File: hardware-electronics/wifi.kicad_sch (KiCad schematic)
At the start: 22 parts, among them J4 CONMHF1-SMD-T, U1 RTL8188FTV-VC-CG, Y5 ABM8-40.000MHZ-B2-T

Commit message: [#17] USB routing plan WIP
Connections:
- net +3V3_wifi: now also R38.1
- net GND: no longer R38.1
- net at U1.23 (LED/GPIO4): now also D4.1 (K); no longer D4.2 (A)
- net at R38.2: now also D4.2 (A); no longer D4.1 (K)
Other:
- moved on the sheet: D4
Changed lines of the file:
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@@
 			)
 		)
-		(property "Datasheet" ""
+		(property "Datasheet" "https://xonstorage.blob.core.windows.net/pdf/realtek_rtl8188ftvvccg_apr22_xonlink.pdf"
 			(at 144.78 96.52 0)
 			(effects
@@
 	)
 	(symbol
+		(lib_id "power:+3V3")
+		(at 93.98 104.14 90)
+		(unit 1)
+		(exclude_from_sim no)
+		(in_bom yes)
+		(on_board yes)
+		(dnp no)
+		(fields_autoplaced yes)
+		(property "Reference" "#PWR0110"
+			(at 97.79 104.14 0)
+			(effects
+				(font
+					(size 1.27 1.27)
+				)
+				(hide yes)
+			)
+		)
+		(property "Value" "+3V3_wifi"
+			(at 90.17 104.1399 90)
+			(effects
+				(font
+					(size 1.27 1.27)
+				)
+				(justify left)
+			)
+		)
+		(property "Footprint" ""
+			(at 93.98 104.14 0)
+			(effects
+				(font
+					(size 1.27 1.27)
+				)
+				(hide yes)
+			)
+		)
+		(property "Datasheet" ""
+			(at 93.98 104.14 0)
+			(effects
+				(font
+					(size 1.27 1.27)
+				)
+				(hide yes)
+			)
+		)
+		(property "Description" "Power symbol creates a global label with name \"+3V3\""
+			(at 93.98 104.14 0)
+			(effects
+				(font
+					(size 1.27 1.27)
+				)
+				(hide yes)
+			)
+		)
+		(pin "1"
+		)
+		(instances
+			(project "M2SmartHome"
+				(path "/da663dec-9e91-4003-a791-431d460ad63c/7a341d5c-2113-408f-a1b4-1e4771333f4d"
+					(reference "#PWR0110")
+					(unit 1)
+				)
+			)
+		)
+	)
+	(symbol
 		(lib_id "M2SmartHomeSymbols:04025A270FAT2A")
 		(at 153.67 163.83 90)
@@
 	(symbol
 		(lib_id "M2SmartHomeSymbols:KP-1608CGCK")
-		(at 111.76 104.14 0)
+		(at 111.76 104.14 180)
 		(unit 1)
 		(exclude_from_sim no)
@@
 		(fields_autoplaced yes)
 		(property "Reference" "D4"
-			(at 110.1725 111.76 0)
+			(at 113.3475 96.52 0)
 			(effects
 				(font
@@
 		)
 		(property "Value" "LED"
-			(at 110.1725 109.22 0)
+			(at 113.3475 99.06 0)
 			(effects
 				(font
@@
 					(unit 1)
 				)
-			)
-		)
-	)
-	(symbol
-		(lib_id "power:GND")
-		(at 93.98 104.14 270)
-		(unit 1)
-		(exclude_from_sim no)
-		(in_bom yes)
-		(on_board yes)
-		(dnp no)
-		(fields_autoplaced yes)
-		(property "Reference" "#PWR0126"
-			(at 87.63 104.14 0)
-			(effects
-				(font
-					(size 1.27 1.27)
-				)
-				(hide yes)
-			)
-		)
-		(property "Value" "GND"
-			(at 90.17 104.1401 90)
-			(effects
-				(font
-					(size 1.27 1.27)
-				)
-				(justify right)
-			)
-		)
-		(property "Footprint" ""
-			(at 93.98 104.14 0)
-			(effects
-				(font
-					(size 1.27 1.27)
-				)
-				(hide yes)
-			)
-		)
-		(property "Datasheet" ""
-			(at 93.98 104.14 0)
-			(effects
-				(font
-					(size 1.27 1.27)
-				)
-				(hide yes)
-			)
-		)
-		(property "Description" "Power symbol creates a global label with name \"GND\" , ground"
-			(at 93.98 104.14 0)
-			(effects
-				(font
-					(size 1.27 1.27)
-				)
-				(hide yes)
-			)
-		)
-		(pin "1"
-		)
-		(instances
-			(project "M2SmartHome"
-				(path "/da663dec-9e91-4003-a791-431d460ad63c/7a341d5c-2113-408f-a1b4-1e4771333f4d"
-					(reference "#PWR0126")
-					(unit 1)
-				)

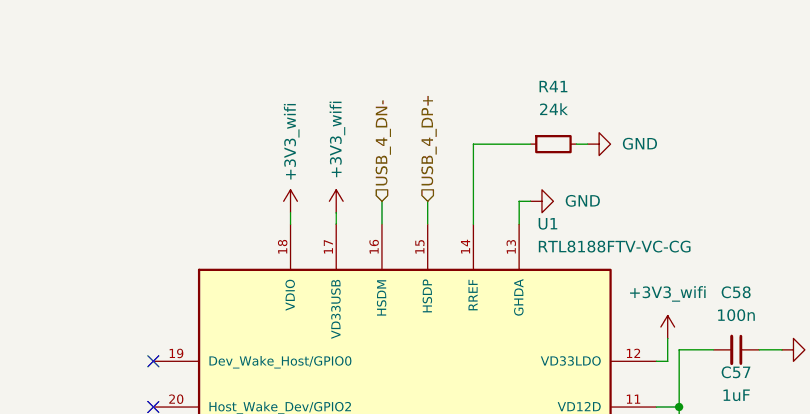
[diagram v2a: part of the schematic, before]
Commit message: [#17] SCH update USB net names
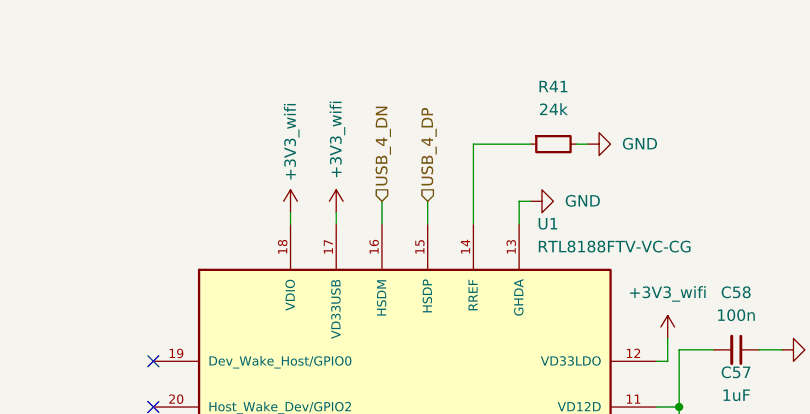
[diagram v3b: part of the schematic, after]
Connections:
- net USB_4_DN- renamed USB_4_DN
- net USB_4_DP+ renamed USB_4_DP
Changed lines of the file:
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@@
 		)
 	)
-	(hierarchical_label "USB_4_DP+"
+	(hierarchical_label "USB_4_DP"
 		(shape input)
 		(at 147.32 66.04 90)
@@
 		)
 	)
-	(hierarchical_label "USB_4_DN-"
+	(hierarchical_label "USB_4_DN"
 		(shape input)
 		(at 142.24 66.04 90)

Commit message: [#20] PCB DRC warnings WIP fix missing footprints
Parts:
- L4: footprint M2SmartHomeFootprints:L_0201_0603Metric -> M2SmartHomeFootprints:L_0201
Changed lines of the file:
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@@
 			)
 		)
-		(property "Footprint" "M2SmartHomeFootprints:L_0201_0603Metric"
+		(property "Footprint" "M2SmartHomeFootprints:L_0201"
 			(at 200.66 121.92 0)
 			(effects

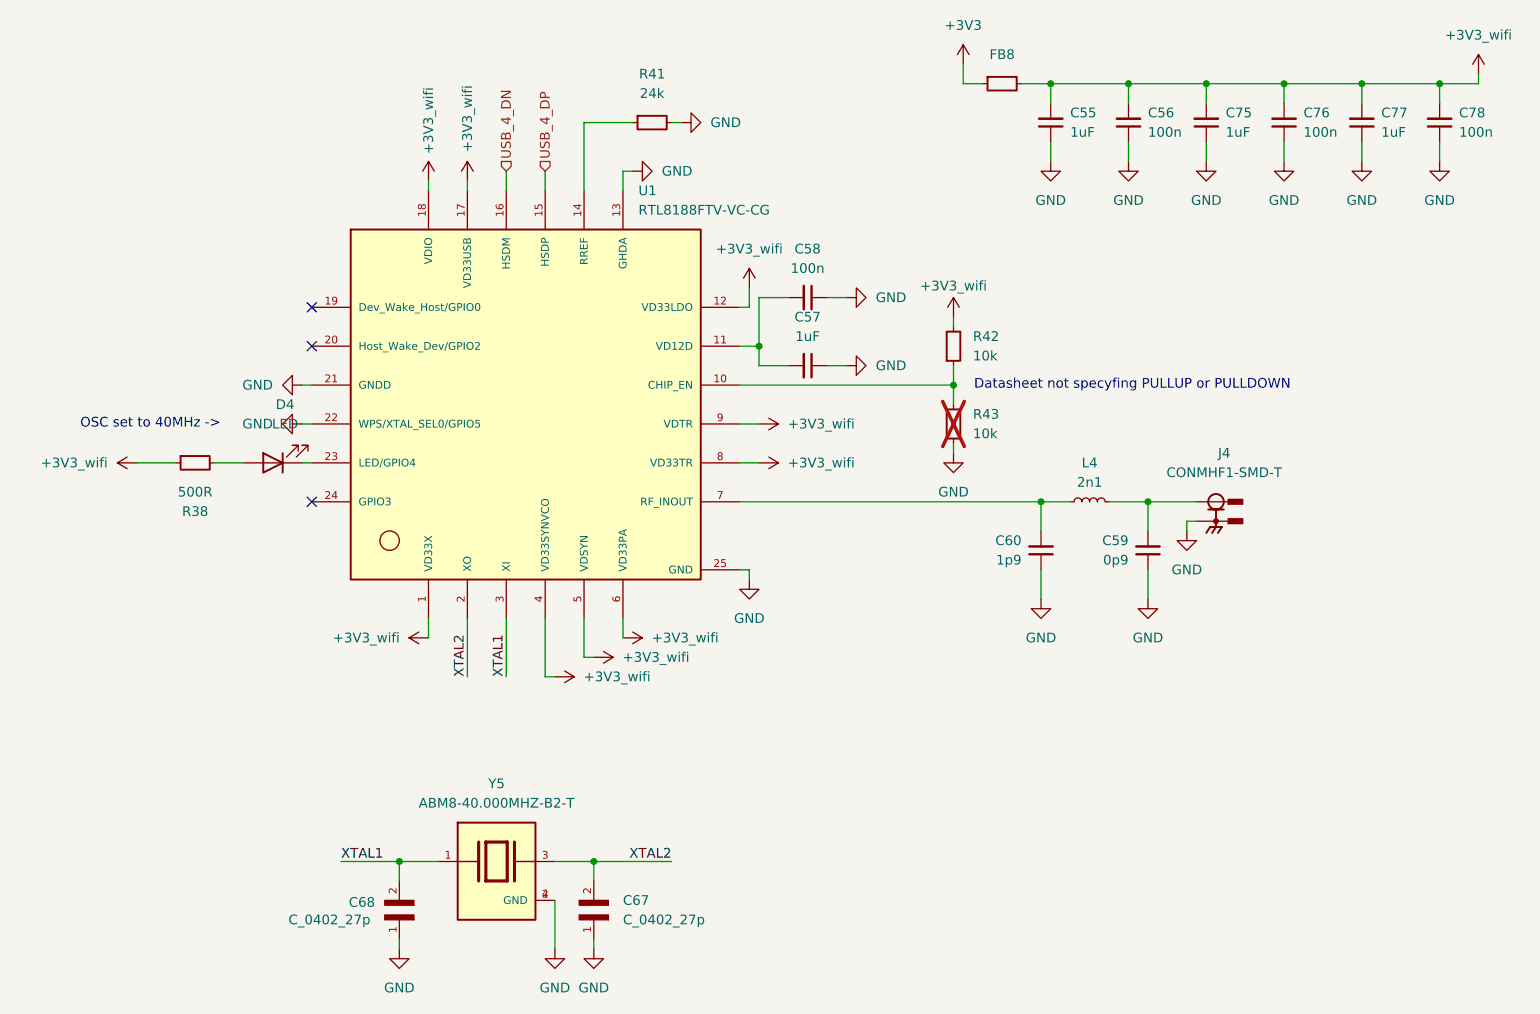
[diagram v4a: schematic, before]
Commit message: [#26] Remove power plane splits for invidual devices
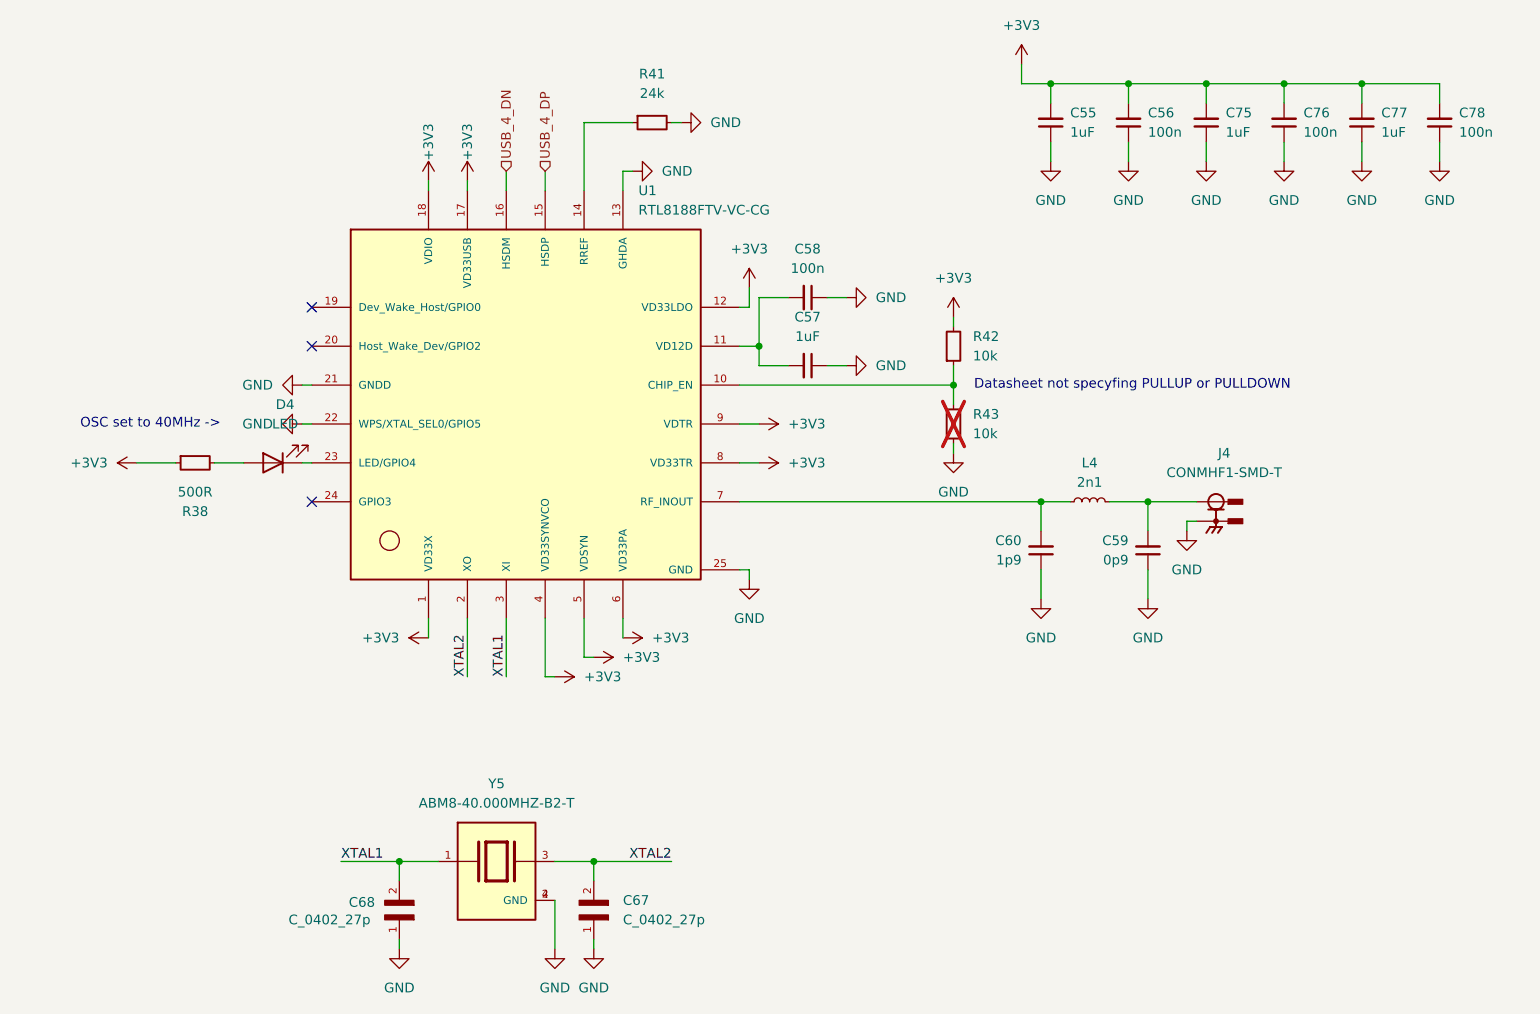
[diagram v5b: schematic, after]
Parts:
- removed FB8: FB_120R_0603, M2SmartHomeFootprints:FB_0603, symbol M2SmartHomeSymbols:FB_120R_0603
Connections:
- net +3V3_wifi is gone; now on net +3V3: C55.2, C56.2, C75.2, C76.2, C77.2, C78.2, R38.1, R42.2, U1.1 (VD33X), U1.12 (VD33LDO), U1.17 (VD33USB), U1.18 (VDIO), U1.4 (VD33SYNVCO), U1.5 (VDSYN), U1.6 (VD33PA), U1.8 (VD33TR), U1.9 (VDTR)

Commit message: [#26] Correct MPN GRM155R61A104KA01D
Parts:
- C56, C58, C76, C78: Author Your Name -> Lukasz Nowarkiewicz; MPN GRM155R61A104KE01D -> GRM155R61A104KA01D
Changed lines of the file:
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@@
 			)
 		)
-		(property "MPN" "GRM155R61A104KE01D"
+		(property "MPN" "GRM155R61A104KA01D"
 			(at 281.94 41.91 0)
 			(effects
@@
 			)
 		)
-		(property "Author" "Your Name"
+		(property "Author" "Lukasz Nowarkiewicz"
 			(at 289.56 41.91 0)
 			(effects
@@
 			)
 		)
-		(property "MPN" "GRM155R61A104KE01D"
+		(property "MPN" "GRM155R61A104KA01D"
 			(at 261.62 41.91 0)
 			(effects
@@
 			)
 		)
-		(property "Author" "Your Name"
+		(property "Author" "Lukasz Nowarkiewicz"
 			(at 269.24 41.91 0)
 			(effects
@@
 			)
 		)
-		(property "MPN" "GRM155R61A104KE01D"
+		(property "MPN" "GRM155R61A104KA01D"
 			(at 241.3 41.91 0)
 			(effects
@@
 			)
 		)
-		(property "Author" "Your Name"
+		(property "Author" "Lukasz Nowarkiewicz"
 			(at 248.92 41.91 0)
 			(effects
@@
 			)
 		)
-		(property "MPN" "GRM155R61A104KE01D"
+		(property "MPN" "GRM155R61A104KA01D"
 			(at 163.83 64.77 0)
 			(effects
@@
 			)
 		)
-		(property "Author" "Your Name"
+		(property "Author" "Lukasz Nowarkiewicz"
 			(at 163.83 57.15 0)
 			(effects

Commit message: [#26] Correct MPN GRM155R61H105KE05D
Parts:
- C55, C57, C75, C77: Author Your Name -> Lukasz Nowarkiewicz; MPN GRM155R61H105KE92D -> GRM155R61H105KE05D
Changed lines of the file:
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@@
 			)
 		)
-		(property "MPN" "GRM155R61H105KE92D"
+		(property "MPN" "GRM155R61H105KE05D"
 			(at 163.83 73.66 0)
 			(effects
@@
 			)
 		)
-		(property "Author" "Your Name"
+		(property "Author" "Lukasz Nowarkiewicz"
 			(at 163.83 66.04 0)
 			(effects
@@
 			)
 		)
-		(property "MPN" "GRM155R61H105KE92D"
+		(property "MPN" "GRM155R61H105KE05D"
 			(at 251.46 41.91 0)
 			(effects
@@
 			)
 		)
-		(property "Author" "Your Name"
+		(property "Author" "Lukasz Nowarkiewicz"
 			(at 259.08 41.91 0)
 			(effects
@@
 			)
 		)
-		(property "MPN" "GRM155R61H105KE92D"
+		(property "MPN" "GRM155R61H105KE05D"
 			(at 231.14 41.91 0)
 			(effects
@@
 			)
 		)
-		(property "Author" "Your Name"
+		(property "Author" "Lukasz Nowarkiewicz"
 			(at 238.76 41.91 0)
 			(effects
@@
 			)
 		)
-		(property "MPN" "GRM155R61H105KE92D"
+		(property "MPN" "GRM155R61H105KE05D"
 			(at 271.78 41.91 0)
 			(effects
@@
 			)
 		)
-		(property "Author" "Your Name"
+		(property "Author" "Lukasz Nowarkiewicz"
 			(at 279.4 41.91 0)
 			(effects

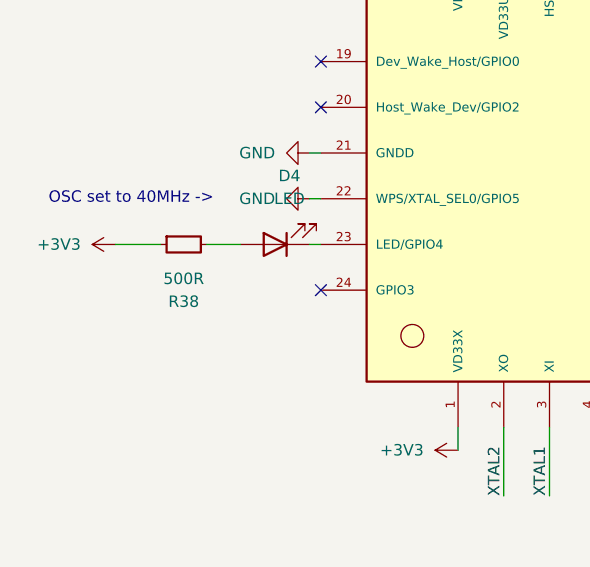
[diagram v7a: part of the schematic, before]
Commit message: [#26] Replace 500ohm to 510ohm  MPN CRCW0402510RJNED
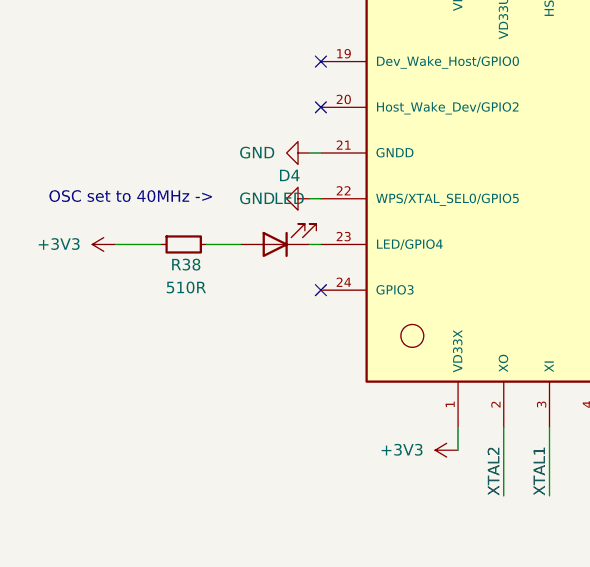
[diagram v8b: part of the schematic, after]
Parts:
- removed R38: R_500R_0402, M2SmartHomeFootprints:R_0402, symbol M2SmartHomeSymbols:R_500R_0402
- added R38: R_510R_0402, M2SmartHomeFootprints:R_0402, symbol M2SmartHomeSymbols:R_510R_0402
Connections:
- net +3V3: now also R38.1
- net at D4.2 (A): now also R38.2
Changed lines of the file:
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@@
 	)
 	(symbol
+		(lib_id "M2SmartHomeSymbols:R_510R_0402")
+		(at 99.06 104.14 0)
+		(unit 1)
+		(exclude_from_sim no)
+		(in_bom yes)
+		(on_board yes)
+		(dnp no)
+		(property "Reference" "R38"
+			(at 101.854 106.426 0)
+			(effects
+				(font
+					(size 1.27 1.27)
+					(thickness 0.15)
+				)
+			)
+		)
+		(property "Value" "R_510R_0402"
+			(at 119.38 116.84 0)
+			(effects
+				(font
+					(size 1.27 1.27)
+					(thickness 0.15)
+				)
+				(justify left bottom)
+				(hide yes)
+			)
+		)
+		(property "Footprint" "M2SmartHomeFootprints:R_0402"
+			(at 119.38 119.38 0)
+			(effects
+				(font
+					(size 1.27 1.27)
+					(thickness 0.15)
+				)
+				(justify left bottom)
+				(hide yes)
+			)
+		)
+		(property "Datasheet" "https://www.vishay.com/docs/20035/crcw0402.pdf"
+			(at 119.38 121.92 0)
+			(effects
+				(font
+					(size 1.27 1.27)
+					(thickness 0.15)
+				)
+				(justify left bottom)
+				(hide yes)
+			)
+		)
+		(property "Description" "SMD Thick Film Resistor, 510 Ω, ±1%, 1/16 W, 0402 [1005 Metric], CRCW Series"
+			(at 99.06 104.14 0)
+			(effects
+				(font
+					(size 1.27 1.27)
+				)
+				(hide yes)
+			)
+		)
+		(property "MPN" "CRCW0402510RJNED"
+			(at 119.38 124.46 0)
+			(effects
+				(font
+					(size 1.27 1.27)
+					(thickness 0.15)
+				)
+				(justify left bottom)
+				(hide yes)
+			)
+		)
+		(property "Manufacturer" "Vishay"
+			(at 119.38 127 0)
+			(effects
+				(font
+					(size 1.27 1.27)
+					(thickness 0.15)
+				)
+				(justify left bottom)
+				(hide yes)
+			)
+		)
+		(property "License" "Apache-2.0"
+			(at 119.38 129.54 0)
+			(effects
+				(font
+					(size 1.27 1.27)
+					(thickness 0.15)
+				)
+				(justify left bottom)
+				(hide yes)
+			)
+		)
+		(property "Author" "Lukasz Nowarkiewicz"
+			(at 119.38 132.08 0)
+			(effects
+				(font
+					(size 1.27 1.27)
+					(thickness 0.15)
+				)
+				(justify left bottom)
+				(hide yes)
+			)
+		)
+		(property "Val" "510R"
+			(at 101.854 108.966 0)
+			(effects
+				(font
+					(size 1.27 1.27)
+					(thickness 0.15)
+				)
+			)
+		)
+		(property "Tolerance" "1%"
+			(at 119.38 114.3 0)
+			(effects
+				(font
+					(size 1.27 1.27)
+				)
+				(justify left bottom)
+				(hide yes)
+			)
+		)
+		(property "Power" "1/16 W"
+			(at 119.38 117.84 0)
+			(effects
+				(font
+					(size 1.27 1.27)
+				)
+				(justify left bottom)
+				(hide yes)
+			)
+		)
+		(pin "2"
+		)
+		(pin "1"
+		)
+		(instances
+			(project "M2SmartHome"
+				(path "/da663dec-9e91-4003-a791-431d460ad63c/7a341d5c-2113-408f-a1b4-1e4771333f4d"
+					(reference "R38")
+					(unit 1)
+				)
+			)
+		)
+	)
+	(symbol
 		(lib_id "power:+3V3")
 		(at 137.16 67.31 0)
@@
 					(unit 1)
 				)
-			)
-		)
-	)
-	(symbol
-		(lib_id "M2SmartHomeSymbols:R_500R_0402")
-		(at 99.06 104.14 0)
-		(unit 1)
-		(exclude_from_sim no)
-		(in_bom yes)
-		(on_board yes)
-		(dnp no)
-		(fields_autoplaced yes)
-		(property "Reference" "R38"
-			(at 101.6 110.49 0)
-			(effects
-				(font
-					(size 1.27 1.27)
-					(thickness 0.15)
-				)
-			)
-		)
-		(property "Value" "R_500R_0402"
-			(at 119.38 116.84 0)
-			(effects
-				(font
-					(size 1.27 1.27)
-					(thickness 0.15)
-				)
-				(justify left bottom)
-				(hide yes)
-			)
-		)
-		(property "Footprint" "M2SmartHomeFootprints:R_0402"
-			(at 119.38 119.38 0)
-			(effects
-				(font
-					(size 1.27 1.27)
-					(thickness 0.15)
-				)
-				(justify left bottom)
-				(hide yes)
-			)
-		)
-		(property "Datasheet" "https://www.vishay.com/docs/20035/crcw0402.pdf"
-			(at 119.38 121.92 0)
-			(effects
-				(font
-					(size 1.27 1.27)
-					(thickness 0.15)
-				)
-				(justify left bottom)
-				(hide yes)
-			)
-		)
-		(property "Description" "SMD Thick Film Resistor, 500 Ω, ±1%, 1/16 W, 0402 [1005 Metric], CRCW Series"
-			(at 99.06 104.14 0)
-			(effects
-				(font
-					(size 1.27 1.27)
-				)
-				(hide yes)
-			)
-		)
-		(property "MPN" "CRCW0402500RFKED"
-			(at 119.38 124.46 0)
-			(effects
-				(font
-					(size 1.27 1.27)
-					(thickness 0.15)
-				)
-				(justify left bottom)
-				(hide yes)
-			)
-		)
-		(property "Manufacturer" "Vishay"
-			(at 119.38 127 0)
-			(effects
-				(font
-					(size 1.27 1.27)
-					(thickness 0.15)
-				)
-				(justify left bottom)
-				(hide yes)
-			)
-		)
-		(property "License" "Apache-2.0"
-			(at 119.38 129.54 0)
-			(effects
-				(font
-					(size 1.27 1.27)
-					(thickness 0.15)
-				)
-				(justify left bottom)
-				(hide yes)
-			)
-		)
-		(property "Author" "Your Name"
-			(at 119.38 132.08 0)
-			(effects
-				(font
-					(size 1.27 1.27)
-					(thickness 0.15)
-				)
-				(justify left bottom)
-				(hide yes)
-			)
-		)
-		(property "Val" "500R"
-			(at 101.6 107.95 0)
-			(effects
-				(font
-					(size 1.27 1.27)
-					(thickness 0.15)
-				)
-			)
-		)
-		(property "Tolerance" "1%"
-			(at 119.38 114.3 0)
-			(effects
-				(font
-					(size 1.27 1.27)
-				)
-				(justify left bottom)
-				(hide yes)
-			)
-		)
-		(property "Power" "1/16 W"
-			(at 119.38 117.84 0)
-			(effects
-				(font
-					(size 1.27 1.27)
-				)
-				(justify left bottom)
-				(hide yes)
-			)
-		)
-		(pin "1"
-		)
-		(pin "2"
-		)
-		(instances
-			(project "M2SmartHome"
-				(path "/da663dec-9e91-4003-a791-431d460ad63c/7a341d5c-2113-408f-a1b4-1e4771333f4d"
-					(reference "R38")
-					(unit 1)
-				)
